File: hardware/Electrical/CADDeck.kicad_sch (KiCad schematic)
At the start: 54 parts, among them J1 Conn_01x05_Socket, J2 Conn_01x05_Pin, J3 Conn_01x04_Pin, J4 Conn_01x04_Socket, J5 Conn_01x10_Socket, J6 Conn_01x10_Pin, Q1 2N2222, SW1 SW_Push, SW10 SW_Push, SW2 SW_Push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

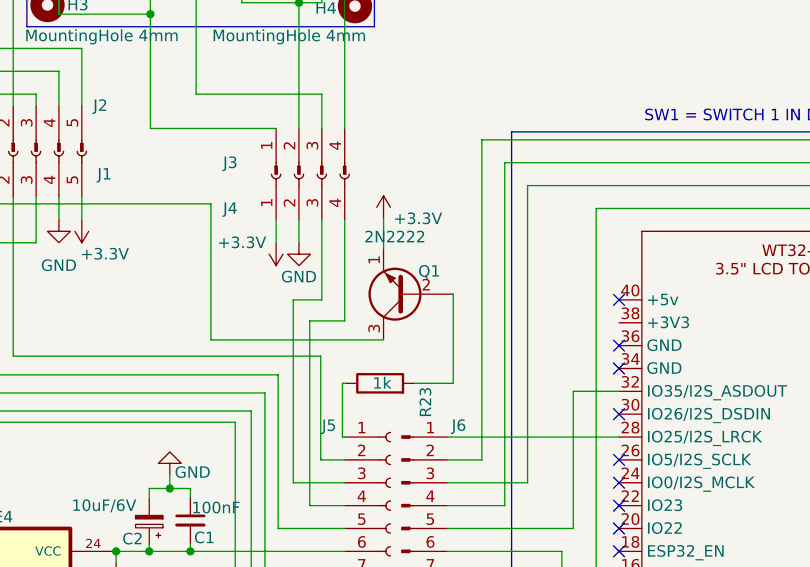
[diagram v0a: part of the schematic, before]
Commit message: NPN durch PNP Transistor getauscht
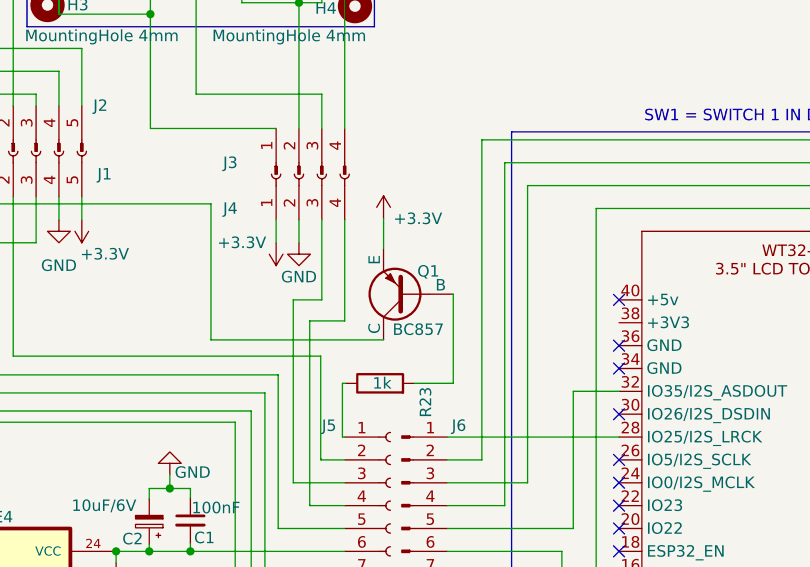
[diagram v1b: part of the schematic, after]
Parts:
- removed Q1: 2N2222, Package_TO_SOT_SMD:TSOT-23, symbol Transistor_BJT:2N2219
- added Q1: BC857, Package_TO_SOT_SMD:SOT-23, symbol Simulation_SPICE:PNP
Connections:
- net +3.3V: now also Q1.3 (E)
- net at R23.2: now also Q1.2 (B)
- net at R13.2, R14.2, R15.2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: now also Q1.1 (C)
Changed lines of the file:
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@@
-    )
-  )
-  (symbol (lib_id "Transistor_BJT:2N2219") (at 185.928 94.615 180) (unit 1)
-    (in_bom yes) (on_board yes) (dnp no)
-    (property "Reference" "Q1" (at 188.468 92.075 0)
-      (effects (font (size 1.27 1.27)))
-    )
-    (property "Value" "2N2222" (at 184.658 88.265 0)
-      (effects (font (size 1.27 1.27)))
-    )
-    (property "Footprint" "Package_TO_SOT_SMD:TSOT-23" (at 180.848 92.71 0)
-      (effects (font (size 1.27 1.27) italic) (justify left) hide)
-    )
-    (property "Datasheet" "http://www.onsemi.com/pub_link/Collateral/2N2219-D.PDF" (at 185.928 94.615 0)
-      (effects (font (size 1.27 1.27)) (justify left) hide)
-    )
-    (pin "1")
-    (pin "2")
-    (pin "3")
-    (instances
-      (project "CADDeck"
-        (path "/35ea3785-d2ac-411c-b2c0-fb3fbf77b703"
-          (reference "Q1") (unit 1)
-        )
-      )
     )
   )
@@
         )
       )
+    )
+  )
+  (symbol (lib_id "Simulation_SPICE:PNP") (at 185.928 94.615 180) (unit 1)
+    (in_bom yes) (on_board yes) (dnp no)
+    (property "Reference" "Q1" (at 189.611 92.075 0)
+      (effects (font (size 1.27 1.27)) (justify left))
+    )
+    (property "Value" "BC857" (at 190.119 98.552 0)
+      (effects (font (size 1.27 1.27)) (justify left))
+    )
+    (property "Footprint" "Package_TO_SOT_SMD:SOT-23" (at 150.368 94.615 0)
+      (effects (font (size 1.27 1.27)) hide)
+    )
+    (property "Datasheet" "~" (at 150.368 94.615 0)
+      (effects (font (size 1.27 1.27)) hide)
+    )
+    (property "Sim.Device" "PNP" (at 185.928 94.615 0)
+      (effects (font (size 1.27 1.27)) hide)
+    )
+    (property "Sim.Type" "GUMMELPOON" (at 185.928 94.615 0)
+      (effects (font (size 1.27 1.27)) hide)
+    )
+    (property "Sim.Pins" "1=C 2=B 3=E" (at 185.928 94.615 0)
+      (effects (font (size 1.27 1.27)) hide)
+    )
+    (pin "1")
+    (pin "2")
+    (pin "3")
+    (instances
+      (project "CADDeck"
+        (path "/35ea3785-d2ac-411c-b2c0-fb3fbf77b703"
+          (reference "Q1") (unit 1)
+        )
+      )

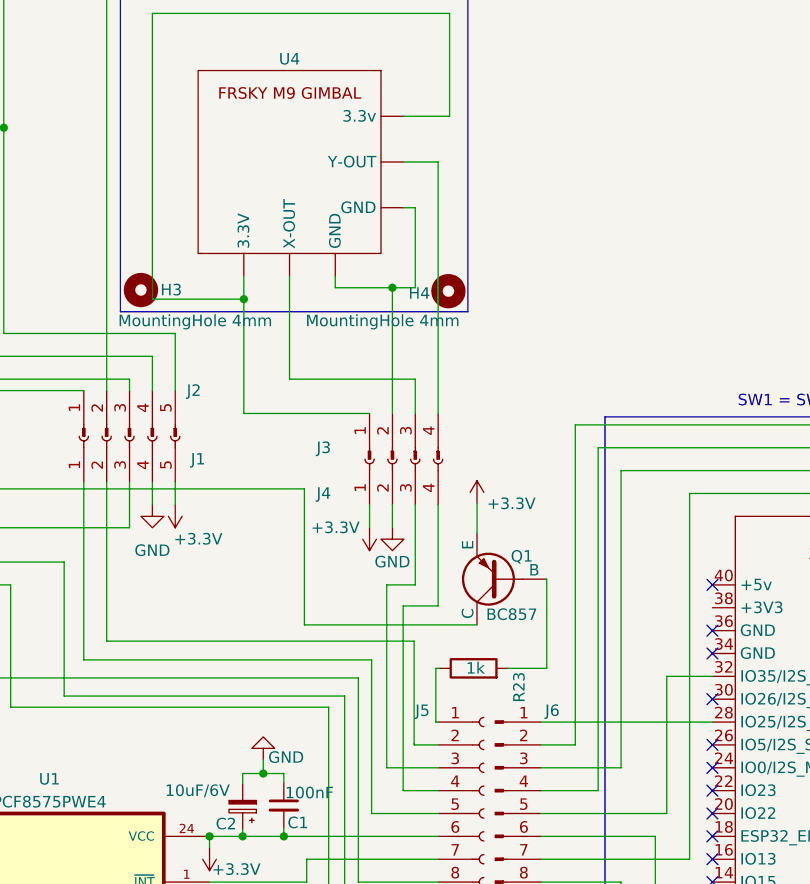
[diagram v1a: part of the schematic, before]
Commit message: LED Ansteuerung
hatte eine falsche Verbindung am Transistor
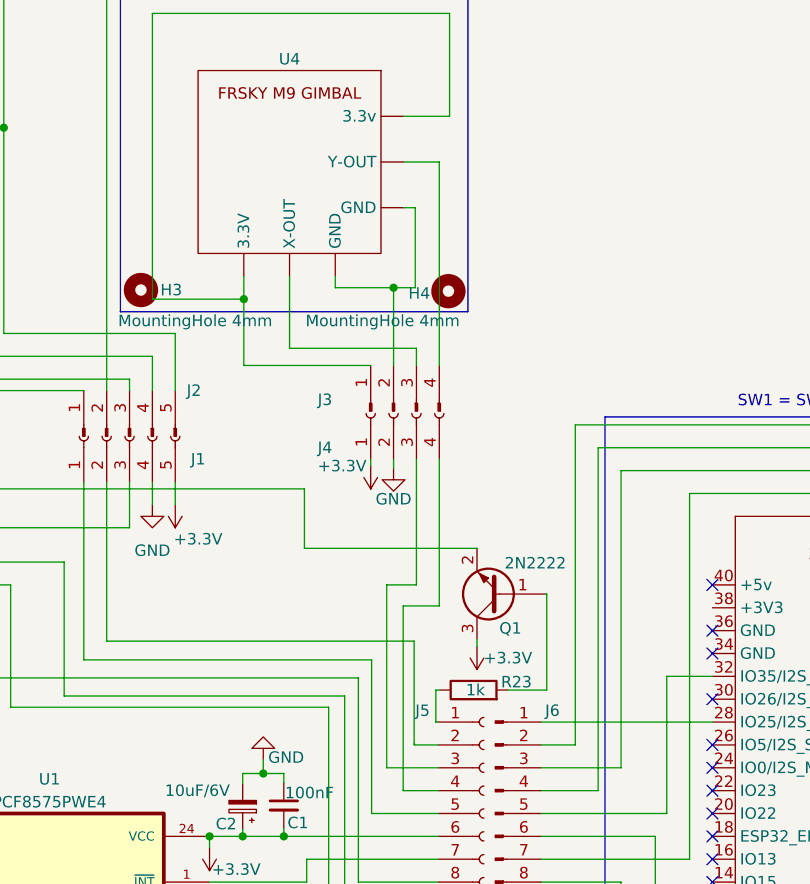
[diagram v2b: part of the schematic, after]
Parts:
- removed Q1: BC857, Package_TO_SOT_SMD:SOT-23, symbol Simulation_SPICE:PNP
- added Q1: 2N2222, Package_TO_SOT_SMD:SOT-23, symbol Transistor_BJT:BC547
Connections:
- net +3.3V: now also Q1.3 (C)
- net at R13.2, R14.2, R15.2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: now also Q1.2 (E)
- net at R23.2: now also Q1.1 (B)
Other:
- moved on the sheet: J3, J4, R23

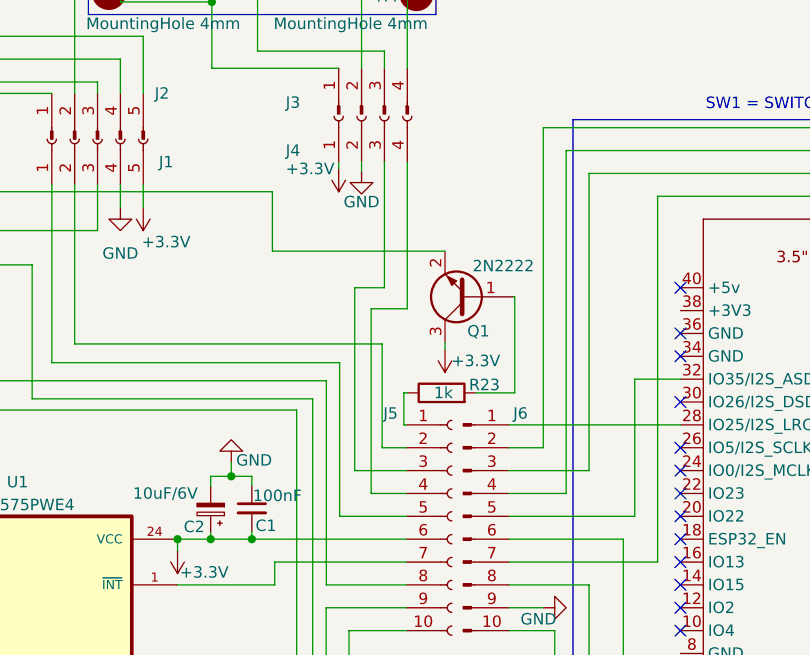
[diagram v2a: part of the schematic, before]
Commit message: Transistor für LED Ansteuerung geändert
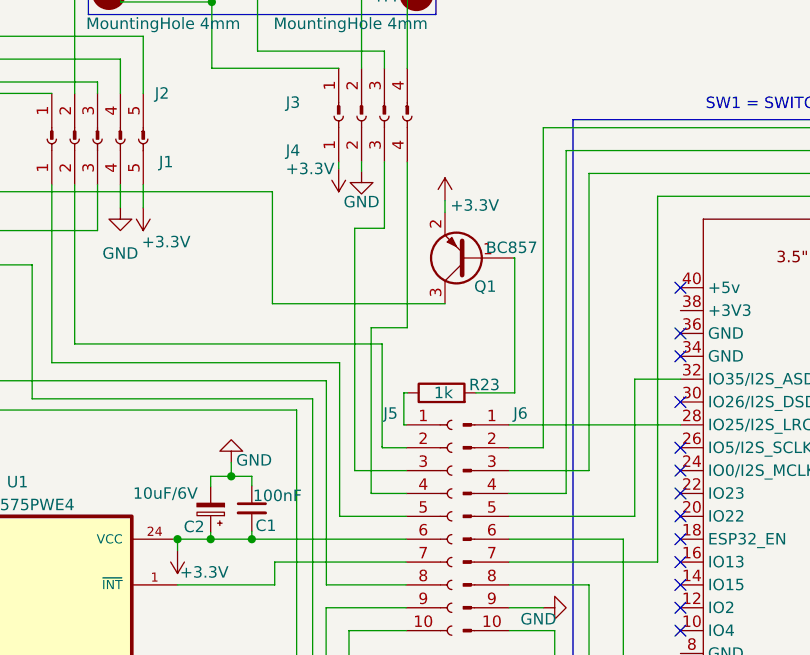
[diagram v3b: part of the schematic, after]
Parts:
- removed Q1: 2N2222, Package_TO_SOT_SMD:SOT-23, symbol Transistor_BJT:BC547
- added Q1: BC857, Package_TO_SOT_SMD:SOT-23, symbol Transistor_BJT:BC857
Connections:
- net +3.3V: now also Q1.2 (E)
- net at R13.2, R14.2, R15.2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: now also Q1.3 (C)
- net at R23.2: now also Q1.1 (B)
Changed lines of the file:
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@@
   (no_connect (at 209.55 125.73))
   (no_connect (at 209.55 95.25))
-  (wire (pts (xy 164.211 91.186) (xy 183.388 91.186))
-    (stroke (width 0) (type default))
-  )
   (wire (pts (xy 20.2184 111.7092) (xy 30.226 111.7092))
     (stroke (width 0) (type default))
@@
     (stroke (width 0) (type default))
   )
-  (wire (pts (xy 191.135 96.266) (xy 191.008 96.266))
+  (wire (pts (xy 191.135 91.948) (xy 191.008 91.948))
     (stroke (width 0) (type default))
   )
@@
     (stroke (width 0) (type default))
   )
+  (wire (pts (xy 164.211 97.028) (xy 183.388 97.028))
+    (stroke (width 0) (type default))
+  )
   (wire (pts (xy 147.32 69.85) (xy 147.32 73.66))
     (stroke (width 0) (type default))
@@
     (stroke (width 0) (type default))
   )
-  (wire (pts (xy 164.211 84.582) (xy 164.211 91.186))
-    (stroke (width 0) (type default))
-  )
   (wire (pts (xy 76.581 113.919) (xy 76.581 110.49))
     (stroke (width 0) (type default))
@@
     (stroke (width 0) (type default))
   )
-  (wire (pts (xy 175.1838 97.5868) (xy 179.197 97.5868))
+  (wire (pts (xy 175.1838 99.695) (xy 179.197 99.695))
     (stroke (width 0) (type default))
   )
@@
     (stroke (width 0) (type default))
   )
-  (wire (pts (xy 175.1838 97.5868) (xy 175.1838 118.0592))
+  (wire (pts (xy 175.1838 99.695) (xy 175.1838 118.0592))
     (stroke (width 0) (type default))
   )
@@
     (stroke (width 0) (type default))
   )
+  (wire (pts (xy 183.388 85.598) (xy 183.388 86.868))
+    (stroke (width 0) (type default))
+  )
   (wire (pts (xy 30.48 139.7) (xy 30.48 144.78))
     (stroke (width 0) (type default))
@@
     (stroke (width 0) (type default))
   )
-  (wire (pts (xy 191.135 96.266) (xy 191.135 106.934))
+  (wire (pts (xy 191.135 91.948) (xy 191.135 106.934))
     (stroke (width 0) (type default))
   )
@@
     (stroke (width 0) (type default))
   )
+  (wire (pts (xy 164.211 84.582) (xy 164.211 97.028))
+    (stroke (width 0) (type default))
+  )
   (wire (pts (xy 261.62 128.27) (xy 250.19 128.27))
     (stroke (width 0) (type default))
@@
     (stroke (width 0) (type default))
   )
-  (wire (pts (xy 176.657 95.25) (xy 176.657 81.28))
+  (wire (pts (xy 176.657 88.646) (xy 176.657 81.28))
     (stroke (width 0) (type default))
   )
@@
     (stroke (width 0) (type default))
   )
-  (wire (pts (xy 173.355 95.25) (xy 176.657 95.25))
+  (wire (pts (xy 173.355 88.646) (xy 176.657 88.646))
     (stroke (width 0) (type default))
   )
@@
     (stroke (width 0) (type default))
   )
-  (wire (pts (xy 173.355 95.25) (xy 173.355 115.57))
+  (wire (pts (xy 173.355 88.646) (xy 173.355 115.57))
     (stroke (width 0) (type default))
   )
@@
     (stroke (width 0) (type default))
   )
-  (wire (pts (xy 183.388 101.346) (xy 183.388 102.108))
-    (stroke (width 0) (type default))
-  )
   (wire (pts (xy 54.61 95.25) (xy 131.572 95.25))
     (stroke (width 0) (type default))
@@
     (stroke (width 0) (type default))
   )
-  (wire (pts (xy 179.197 97.5868) (xy 179.197 81.28))
+  (wire (pts (xy 179.197 99.695) (xy 179.197 81.28))
     (stroke (width 0) (type default))
   )
@@
     )
   )
-  (symbol (lib_id "power:+3.3V") (at 183.388 102.108 180) (unit 1)
+  (symbol (lib_id "power:+3.3V") (at 183.388 85.598 0) (unit 1)
     (in_bom yes) (on_board yes) (dnp no)
-    (property "Reference" "#PWR017" (at 183.388 98.298 0)
+    (property "Reference" "#PWR017" (at 183.388 89.408 0)
       (effects (font (size 1.27 1.27)) hide)
     )
-    (property "Value" "+3.3V" (at 186.817 103.378 0)
+    (property "Value" "+3.3V" (at 186.69 86.106 0)
       (effects (font (size 1.27 1.27)))
     )
-    (property "Footprint" "" (at 183.388 102.108 0)
+    (property "Footprint" "" (at 183.388 85.598 0)
       (effects (font (size 1.27 1.27)) hide)
     )
-    (property "Datasheet" "" (at 183.388 102.108 0)
+    (property "Datasheet" "" (at 183.388 85.598 0)
       (effects (font (size 1.27 1.27)) hide)
     )
@@
     )
   )
-  (symbol (lib_id "Transistor_BJT:BC547") (at 185.928 96.266 180) (unit 1)
-    (in_bom yes) (on_board yes) (dnp no)
-    (property "Reference" "Q1" (at 188.341 100.076 0)
-      (effects (font (size 1.27 1.27)) (justify left))
-    )
-    (property "Value" "2N2222" (at 193.294 92.837 0)
-      (effects (font (size 1.27 1.27)) (justify left))
-    )
-    (property "Footprint" "Package_TO_SOT_SMD:SOT-23" (at 180.848 94.361 0)
-      (effects (font (size 1.27 1.27) italic) (justify left) hide)
-    )
-    (property "Datasheet" "https://www.onsemi.com/pub/Collateral/BC550-D.pdf" (at 185.928 96.266 0)
-      (effects (font (size 1.27 1.27)) (justify left) hide)
-    )
-    (pin "3")
-    (pin "1")
-    (pin "2")
-    (instances
-      (project "CADDeck"
-        (path "/35ea3785-d2ac-411c-b2c0-fb3fbf77b703"
-          (reference "Q1") (unit 1)
-        )
-      )
-    )
-  )
   (symbol (lib_name "SW_Push_1") (lib_id "Switch:SW_Push") (at 30.48 106.045 90) (unit 1)
     (in_bom yes) (on_board yes) (dnp no)
@@
         )
       )
+    )
+  )
+  (symbol (lib_id "Transistor_BJT:BC857") (at 185.928 91.948 180) (unit 1)
+    (in_bom yes) (on_board yes) (dnp no)
+    (property "Reference" "Q1" (at 189.103 95.123 0)
+      (effects (font (size 1.27 1.27)) (justify left))
+    )
+    (property "Value" "BC857" (at 193.675 90.805 0)
+      (effects (font (size 1.27 1.27)) (justify left))
+    )
+    (property "Footprint" "Package_TO_SOT_SMD:SOT-23" (at 180.848 90.043 0)
+      (effects (font (size 1.27 1.27) italic) (justify left) hide)
+    )
+    (property "Datasheet" "https://www.onsemi.com/pub/Collateral/BC860-D.pdf" (at 185.928 91.948 0)
+      (effects (font (size 1.27 1.27)) (justify left) hide)
+    )
+    (pin "1")
+    (pin "2")
+    (pin "3")
+    (instances
+      (project "CADDeck"
+        (path "/35ea3785-d2ac-411c-b2c0-fb3fbf77b703"
+          (reference "Q1") (unit 1)
+        )
+      )

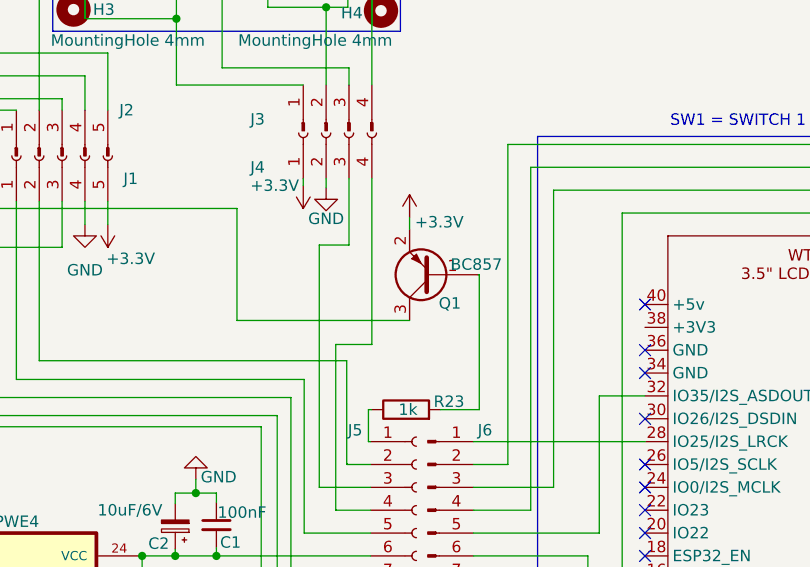
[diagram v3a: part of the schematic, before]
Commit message: Transistor geändert
Bei KiCad war ein fehlerhafter Footprint.
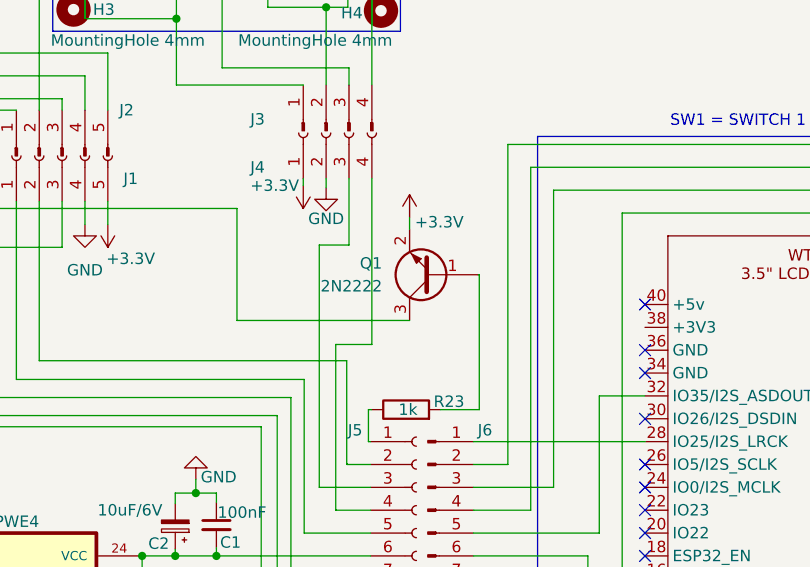
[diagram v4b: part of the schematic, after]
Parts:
- removed Q1: BC857, Package_TO_SOT_SMD:SOT-23, symbol Transistor_BJT:BC857
- added Q1: 2N2222, Package_TO_SOT_SMD:SOT-23, symbol Transistor_BJT:MMBT3904
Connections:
- net +3.3V: now also Q1.2 (E)
- net at R13.2, R14.2, R15.2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: now also Q1.3 (C)
- net at R23.2: now also Q1.1 (B)
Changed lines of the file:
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@@
+    )
+  )
+  (symbol (lib_id "Transistor_BJT:MMBT3904") (at 185.928 91.948 180) (unit 1)
+    (in_bom yes) (on_board yes) (dnp no) (fields_autoplaced)
+    (property "Reference" "Q1" (at 180.34 90.678 0)
+      (effects (font (size 1.27 1.27)) (justify left))
+    )
+    (property "Value" "2N2222" (at 180.34 93.218 0)
+      (effects (font (size 1.27 1.27)) (justify left))
+    )
+    (property "Footprint" "Package_TO_SOT_SMD:SOT-23" (at 180.848 90.043 0)
+      (effects (font (size 1.27 1.27) italic) (justify left) hide)
+    )
+    (property "Datasheet" "https://www.onsemi.com/pub/Collateral/2N3903-D.PDF" (at 185.928 91.948 0)
+      (effects (font (size 1.27 1.27)) (justify left) hide)
+    )
+    (pin "1")
+    (pin "2")
+    (pin "3")
+    (instances
+      (project "CADDeck"
+        (path "/35ea3785-d2ac-411c-b2c0-fb3fbf77b703"
+          (reference "Q1") (unit 1)
+        )
+      )
     )
   )
@@
         )
       )
-    )
-  )
-  (symbol (lib_id "Transistor_BJT:BC857") (at 185.928 91.948 180) (unit 1)
-    (in_bom yes) (on_board yes) (dnp no)
-    (property "Reference" "Q1" (at 189.103 95.123 0)
-      (effects (font (size 1.27 1.27)) (justify left))
-    )
-    (property "Value" "BC857" (at 193.675 90.805 0)
-      (effects (font (size 1.27 1.27)) (justify left))
-    )
-    (property "Footprint" "Package_TO_SOT_SMD:SOT-23" (at 180.848 90.043 0)
-      (effects (font (size 1.27 1.27) italic) (justify left) hide)
-    )
-    (property "Datasheet" "https://www.onsemi.com/pub/Collateral/BC860-D.pdf" (at 185.928 91.948 0)
-      (effects (font (size 1.27 1.27)) (justify left) hide)
-    )
-    (pin "1")
-    (pin "2")
-    (pin "3")
-    (instances
-      (project "CADDeck"
-        (path "/35ea3785-d2ac-411c-b2c0-fb3fbf77b703"
-          (reference "Q1") (unit 1)
-        )
-      )

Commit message: PCG8575 A0-A1 auf GND gelegt
Muss noch getestet werden, da der PCF nicht funktionierte.
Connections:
- net GND: now also U1.2 (A1), U1.21 (A0), U1.3 (A2)
- no-connect marks 37 -> 34
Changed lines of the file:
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@@
   (junction (at 34.29 154.94) (diameter 0) (color 0 0 0 0)
   )
+  (junction (at 118.11 128.27) (diameter 0) (color 0 0 0 0)
+  )
   (junction (at 37.465 113.919) (diameter 0) (color 0 0 0 0)
   )
@@
   )
   (junction (at 16.51 121.92) (diameter 0) (color 0 0 0 0)
+  )
+  (junction (at 118.11 130.81) (diameter 0) (color 0 0 0 0)
   )
   (junction (at 58.42 111.76) (diameter 0) (color 0 0 0 0)
@@
   (no_connect (at 209.55 115.57))
   (no_connect (at 209.55 143.51))
-  (no_connect (at 118.11 133.35))
   (no_connect (at 250.19 140.97))
   (no_connect (at 250.19 97.79))
@@
   (no_connect (at 250.19 102.87))
   (no_connect (at 118.11 158.75))
-  (no_connect (at 118.11 128.27))
-  (no_connect (at 118.11 130.81))
   (no_connect (at 250.19 143.51))
   (no_connect (at 153.67 158.75))
@@
     (stroke (width 0) (type default))
   )
+  (wire (pts (xy 118.11 128.27) (xy 118.11 130.81))
+    (stroke (width 0) (type default))
+  )
   (wire (pts (xy 23.7744 110.5408) (xy 23.7744 113.919))
     (stroke (width 0) (type default))
@@
     (stroke (width 0) (type default))
   )
+  (wire (pts (xy 118.11 130.81) (xy 118.11 133.35))
+    (stroke (width 0) (type default))
+  )
   (wire (pts (xy 30.226 111.76) (xy 30.48 111.76))
     (stroke (width 0) (type default))
@@
   )
   (wire (pts (xy 63.5 179.6796) (xy 63.5 180.975))
+    (stroke (width 0) (type default))
+  )
+  (wire (pts (xy 118.11 125.73) (xy 118.11 128.27))
     (stroke (width 0) (type default))
   )
@@
         )
       )
+    )
+  )
+  (symbol (lib_id "power:GND") (at 118.11 125.73 180) (unit 1)
+    (in_bom yes) (on_board yes) (dnp no) (fields_autoplaced)
+    (property "Reference" "#PWR019" (at 118.11 119.38 0)
+      (effects (font (size 1.27 1.27)) hide)
+    )
+    (property "Value" "GND" (at 118.11 120.65 0)
+      (effects (font (size 1.27 1.27)))
+    )
+    (property "Footprint" "" (at 118.11 125.73 0)
+      (effects (font (size 1.27 1.27)) hide)
+    )
+    (property "Datasheet" "" (at 118.11 125.73 0)
+      (effects (font (size 1.27 1.27)) hide)
+    )
+    (pin "1")
+    (instances
+      (project "CADDeck"
+        (path "/35ea3785-d2ac-411c-b2c0-fb3fbf77b703"
+          (reference "#PWR019") (unit 1)
+        )
+      )
